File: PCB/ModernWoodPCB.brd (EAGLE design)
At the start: 428.5 x 125 mm, 235 parts, among them Q2 FS8205, U1 ESP32-S3HOLE, U2 ME6211C33M5G

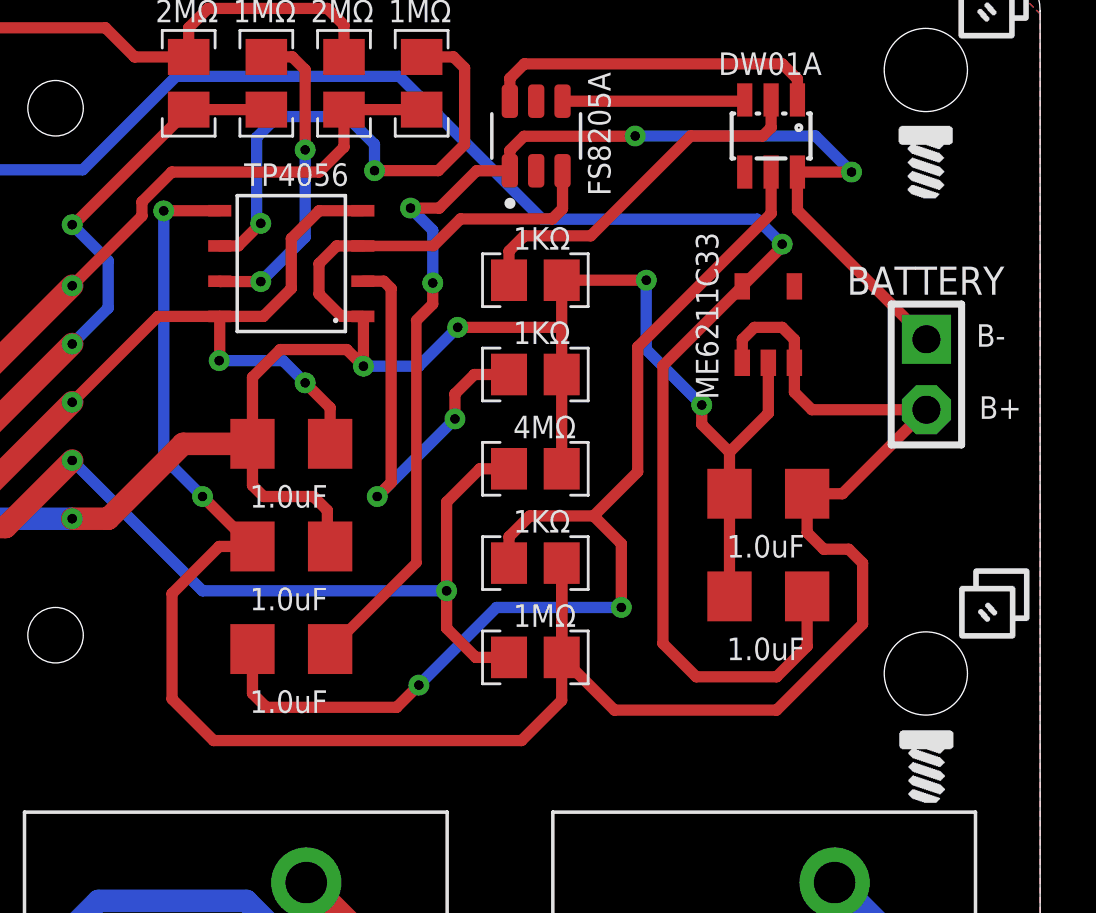
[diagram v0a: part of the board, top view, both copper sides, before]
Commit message: New review of Schematic and added a voltage regulator diode protection
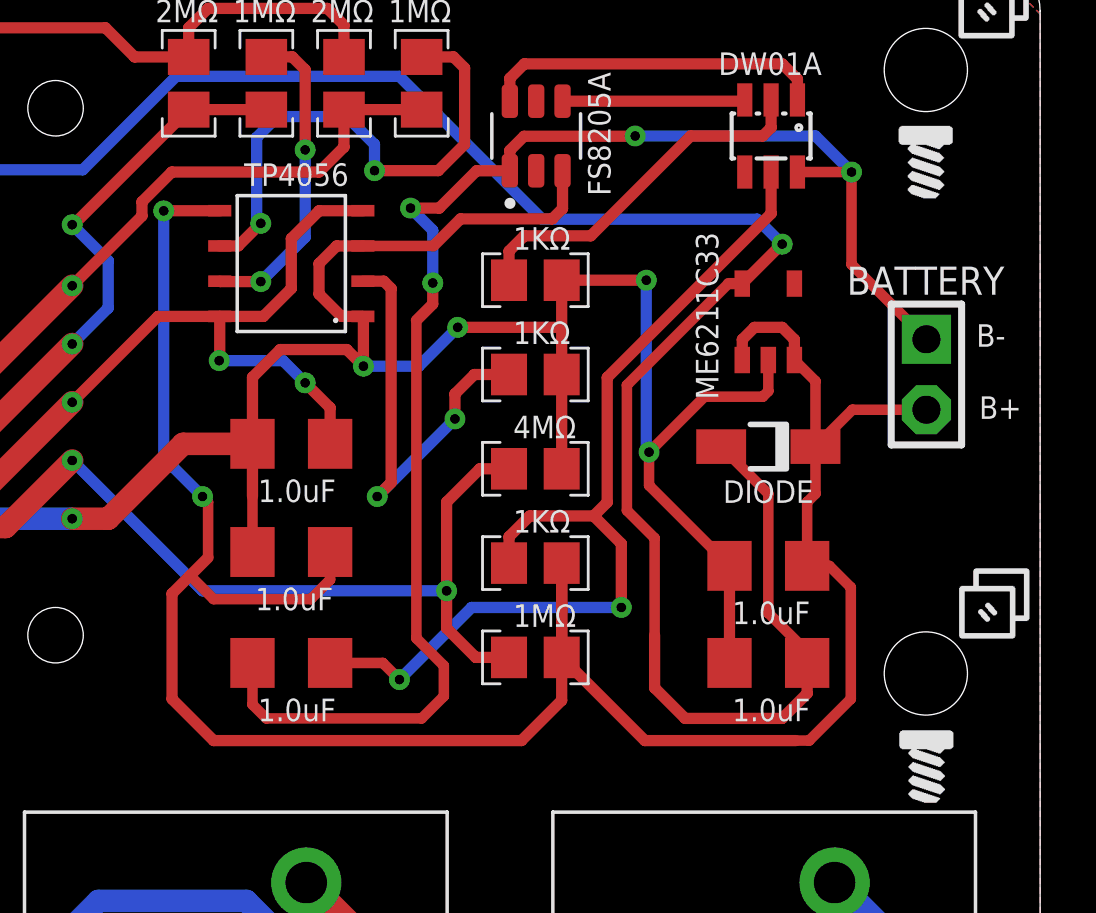
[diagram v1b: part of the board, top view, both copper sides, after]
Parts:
- added DIODE: (no value), bt_diode:SOD123FL
- moved C3 2.60 mm to (421.2, 105.0)
- moved C5 2.40 mm to (421.2, 101.5)
- moved C2 0.50 mm to (404.0, 101.5), turned to 180 degrees
- moved C1 0.20 mm to (404.0, 105.5), turned to 180 degrees
- moved U2 0.10 mm to (421.2, 113.8)
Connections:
- net B+: now also DIODE.C
- net VCC: now also DIODE.A
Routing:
- net VCC: track 501.6 -> 513.1 mm
- net B-: track 45.6 -> 54.6 mm
- net DWVCC: track 39.7 -> 34.9 mm
- net B+: track 81.0 -> 85.5 mm
- net GND: track 715.8 -> 718.7 mm
